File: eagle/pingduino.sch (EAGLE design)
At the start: 35 parts, among them IC1 ATMEGA328, IC3 74LS595N, IC4 74LS595N, IC5 74LS595N, IC6 74LS595N, IC7 74HC14N, Q1 16MHz

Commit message: Fix display connectors on schematic
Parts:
- removed U$1, U$2, U$3, U$4: AVR_SPI_PROG2PTH2, SparkFun-Connectors:AVR_SPI_PROG2PTH2
- added JP2, JP3, JP4, JP5: M05X2SHD, SparkFun-Connectors:M05X2SHD
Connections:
- removed net N$1: IC5.QB, U$3.6
- removed net N$13: IC3.QH, U$1.1
- removed net N$14: IC3.QG, U$1.3
- removed net N$15: IC3.QF, U$1.5
- removed net N$16: IC3.QE, U$1.9
- removed net N$17: IC3.QD, U$1.10
- removed net N$18: IC3.QC, U$1.8
- removed net N$19: IC3.QB, U$1.6
- removed net N$20: IC3.QA, U$1.4
- removed net N$21: IC4.QB, U$2.6
- removed net N$22: IC4.QA, U$2.4
- removed net N$23: IC4.QC, U$2.8
- removed net N$24: IC4.QD, U$2.10
- removed net N$25: IC4.QH, U$2.1
- removed net N$26: IC4.QG, U$2.3
- removed net N$27: IC4.QF, U$2.5
- removed net N$28: IC5.QC, U$3.8
- removed net N$29: IC5.QD, U$3.10
- removed net N$30: IC5.QA, U$3.4
- removed net N$31: IC5.QE, U$3.9
- removed net N$32: IC5.QF, U$3.5
- removed net N$33: IC5.QG, U$3.3
- removed net N$34: IC5.QH, U$3.1
- removed net N$35: IC6.QB, U$4.6
- removed net N$36: IC6.QC, U$4.8
- removed net N$37: IC6.QA, U$4.4
- removed net N$38: IC6.QD, U$4.10
- removed net N$39: IC6.QE, U$4.9
- removed net N$40: IC6.QF, U$4.5
- removed net N$41: IC6.QG, U$4.3
- removed net N$42: IC6.QH, U$4.1
- removed net N$44: IC4.QE, U$2.9
- new net D1A: IC3.QA, JP2.1
- new net D1B: IC3.QB, JP2.2
- new net D1C: IC3.QC, JP2.3
- new net D1D: IC3.QD, JP2.4
- new net D1E: IC3.QE, JP2.5
- new net D1F: IC3.QF, JP2.6
- new net D1G: IC3.QG, JP2.7
- new net D1P: IC3.QH, JP2.8
- new net D2A: IC4.QA, JP3.1
- new net D2B: IC4.QB, JP3.2
- new net D2C: IC4.QC, JP3.3
- new net D2D: IC4.QD, JP3.4
- new net D2E: IC4.QE, JP3.5
- new net D2F: IC4.QF, JP3.6
- new net D2G: IC4.QG, JP3.7
- new net D3A: IC5.QA, JP4.1
- new net D3B: IC5.QB, JP4.2
- new net D3C: IC5.QC, JP4.3
- new net D3D: IC5.QD, JP4.4
- new net D3E: IC5.QE, JP4.5
- new net D3F: IC5.QF, JP4.6
- new net D3G: IC5.QG, JP4.7
- new net D3P: IC5.QH, JP4.8
- new net D4A: IC6.QA, JP5.1
- new net D4B: IC6.QB, JP5.2
- new net D4C: IC6.QC, JP5.3
- new net D4D: IC6.QD, JP5.4
- new net D4E: IC6.QE, JP5.5
- new net D4F: IC6.QF, JP5.6
- new net D4G: IC6.QG, JP5.7
- net GND: now also JP2.10, JP3.10, JP4.10, JP5.10; no longer U$1.7, U$2.7, U$3.7, U$4.7
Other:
- moved on the sheet: IC4, IC5, IC6

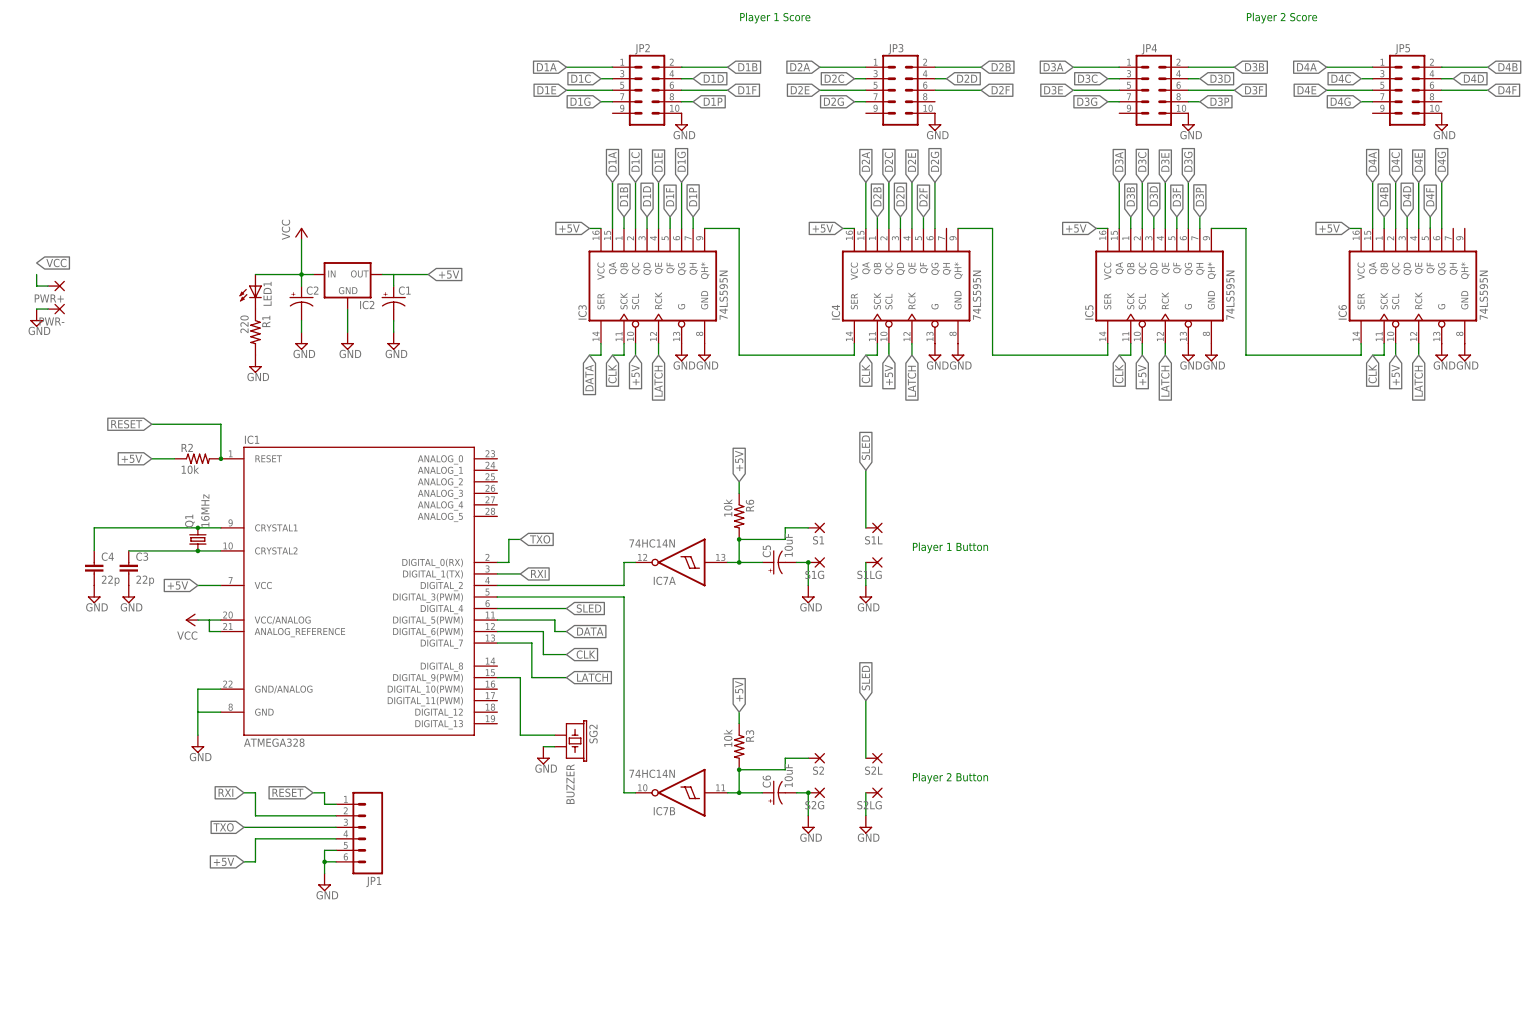
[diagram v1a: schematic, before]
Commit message: Add Garan audio module and amplifier to schematic and board
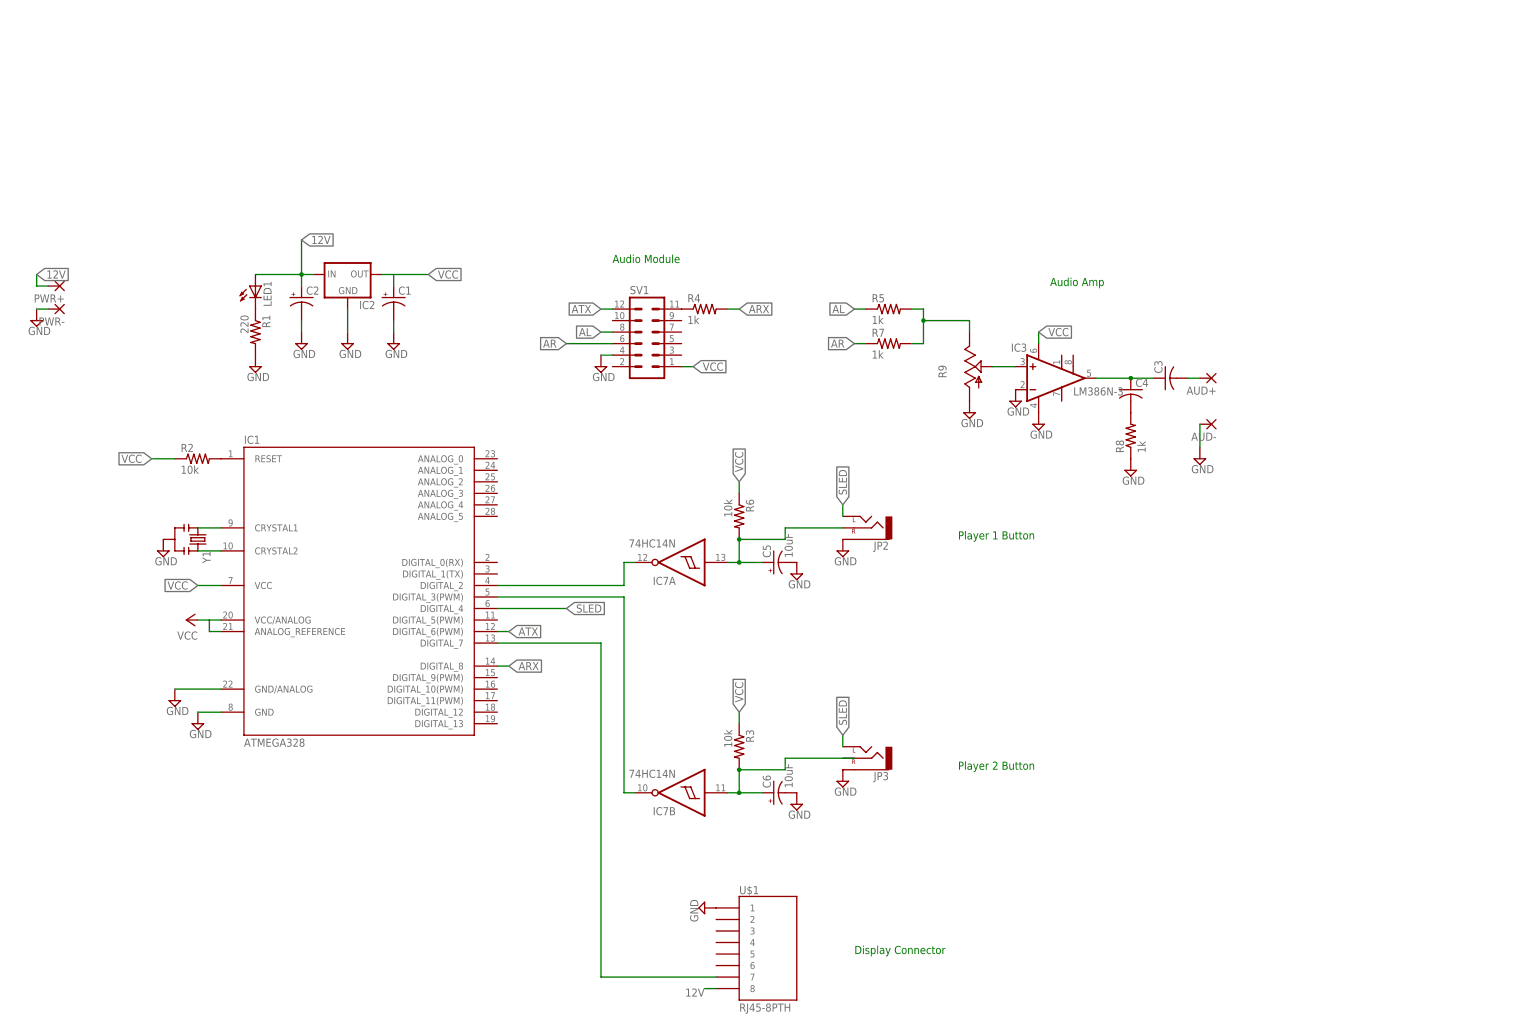
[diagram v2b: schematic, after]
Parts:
- removed IC4, IC5, IC6: 74LS595N, SparkFun-DigitalIC:74LS595N
- removed JP1: (no value), SparkFun-Connectors:M06SIP
- removed JP4, JP5: M05X2SHD, SparkFun-Connectors:M05X2SHD
- removed Q1: 16MHz, adafruit:CRYSTALHC49U-V
- removed S1, S1G, S1L, S1LG, S2, S2G, S2L, S2LG: WIREPAD2,15/1,0, wirepad:WIREPAD2,15/1,0
- removed SG2: BUZZER, SparkFun-Electromechanical:BUZZERPTH
- added AUD+, AUD-: WIREPAD2,15/1,0, wirepad:WIREPAD2,15/1,0
- added R4, R5, R7, R8: 1k, resistor:R-US_0204/7
- added R9: (no value), pot:TRIM_US-B25U
- added SV1: (no value), con-lstb:MA06-2
- added U$1: RJ45-8PTH, SparkFun-Connectors:RJ45-8PTH
- added Y1: (no value), SparkFun-FreqCtrl:RESONATORPTH
- C3, C4: value 22p -> (none); device SparkFun-Capacitors:CAPKIT -> rcl:C-US050-024X044
- IC3: value 74LS595N -> LM386N-3; device SparkFun-DigitalIC:74LS595N -> linear:LM386N-3
- JP2, JP3: value M05X2SHD -> (none); device SparkFun-Connectors:M05X2SHD -> SparkFun-Connectors:AUDIO-JACKPTH
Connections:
- removed net +5V: C1.+, IC1.VCC, IC2.OUT, IC3.SCL, IC3.VCC, IC4.SCL, IC4.VCC, IC5.SCL, IC5.VCC, IC6.SCL, IC6.VCC, JP1.4, R2.1, R3.1, R6.1
- removed net CLK: IC1.DIGITAL_6(PWM), IC3.SCK, IC4.SCK, IC5.SCK, IC6.SCK
- removed net D1A: IC3.QA, JP2.1
- removed net D1B: IC3.QB, JP2.2
- removed net D1C: IC3.QC, JP2.3
- removed net D1D: IC3.QD, JP2.4
- removed net D1E: IC3.QE, JP2.5
- removed net D1F: IC3.QF, JP2.6
- removed net D1G: IC3.QG, JP2.7
- removed net D1P: IC3.QH, JP2.8
- removed net D2A: IC4.QA, JP3.1
- removed net D2B: IC4.QB, JP3.2
- removed net D2C: IC4.QC, JP3.3
- removed net D2D: IC4.QD, JP3.4
- removed net D2E: IC4.QE, JP3.5
- removed net D2F: IC4.QF, JP3.6
- removed net D2G: IC4.QG, JP3.7
- removed net D3A: IC5.QA, JP4.1
- removed net D3B: IC5.QB, JP4.2
- removed net D3C: IC5.QC, JP4.3
- removed net D3D: IC5.QD, JP4.4
- removed net D3E: IC5.QE, JP4.5
- removed net D3F: IC5.QF, JP4.6
- removed net D3G: IC5.QG, JP4.7
- removed net D3P: IC5.QH, JP4.8
- removed net D4A: IC6.QA, JP5.1
- removed net D4B: IC6.QB, JP5.2
- removed net D4C: IC6.QC, JP5.3
- removed net D4D: IC6.QD, JP5.4
- removed net D4E: IC6.QE, JP5.5
- removed net D4F: IC6.QF, JP5.6
- removed net D4G: IC6.QG, JP5.7
- removed net DATA: IC1.DIGITAL_5(PWM), IC3.SER
- removed net LATCH: IC1.DIGITAL_7, IC3.RCK, IC4.RCK, IC5.RCK, IC6.RCK
- removed net N$11: IC4.QH*, IC5.SER
- removed net N$9: IC1.DIGITAL_9(PWM), SG2.1
- removed net RESET: IC1.RESET, JP1.1, R2.2
- removed net RXI: IC1.DIGITAL_1(TX), JP1.2
- removed net TXO: IC1.DIGITAL_0(RX), JP1.3
- new net 12V: C2.+, IC2.IN, LED1.A, PWR+.P, U$1.8
- new net AL: R5.1, SV1.8
- new net AR: R7.1, SV1.6
- new net ARX: IC1.DIGITAL_7, IC1.DIGITAL_8, R4.2, U$1.7
- new net ATX: IC1.DIGITAL_6(PWM), SV1.12
- new net N$1: IC1.CRYSTAL2, Y1.3
- new net N$14: IC3.+IN, R9.S
- new net N$16: C3.1, C4.1, IC3.OUT
- new net N$17: C4.2, R8.2
- new net N$18: AUD+.P, C3.2
- net GND: now also AUD-.P, IC3.-IN, JP2.SLEEVE, JP3.SLEEVE, R8.1, R9.A, SV1.4, U$1.1, Y1.2; no longer C3.2, C4.2, IC3.G, IC4.G, IC4.GND, IC5.G, IC5.GND, IC6.G, IC6.GND, JP1.5, JP1.6, JP2.10, JP3.10, JP4.10, JP5.10, S1G.P, S1LG.P, S2G.P, S2LG.P, SG2.2
- net N$10: now also R4.1, SV1.11; no longer IC3.QH*, IC4.SER
- net N$12: now also R5.2, R7.2, R9.E; no longer IC5.QH*, IC6.SER
- net N$2: now also Y1.1; no longer C4.1, Q1.2
- net N$4: now also IC1.RESET, R2.2; no longer C3.1, IC1.CRYSTAL2, Q1.1
- net N$6: no longer S2.P
- net N$8: now also JP2.RIGHT; no longer S1.P
- net SLED: now also JP2.LEFT, JP3.LEFT; no longer S1L.P, S2L.P
- net VCC: now also C1.+, IC1.VCC, IC2.OUT, IC3.VS, R2.1, R3.1, R6.1, SV1.1; no longer C2.+, IC2.IN, LED1.A, PWR+.P
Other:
- note added: "Audio Amp"
- note added: "Audio Module"
- note added: "Display Connector"
- note removed: "Player 1 Score"
- note removed: "Player 2 Score"
- moved on the sheet: C3, C4
